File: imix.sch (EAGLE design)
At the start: 161 parts, among them Q1 AO3418, Q2 AO3415, Q3 AO3415, Q4 AO3415, Q5 AO3415, U1 BQ2423X, U10 ISL29035, U11 FX0S8700CQ, U12 296-12686-1-ND, U3 TLV3202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

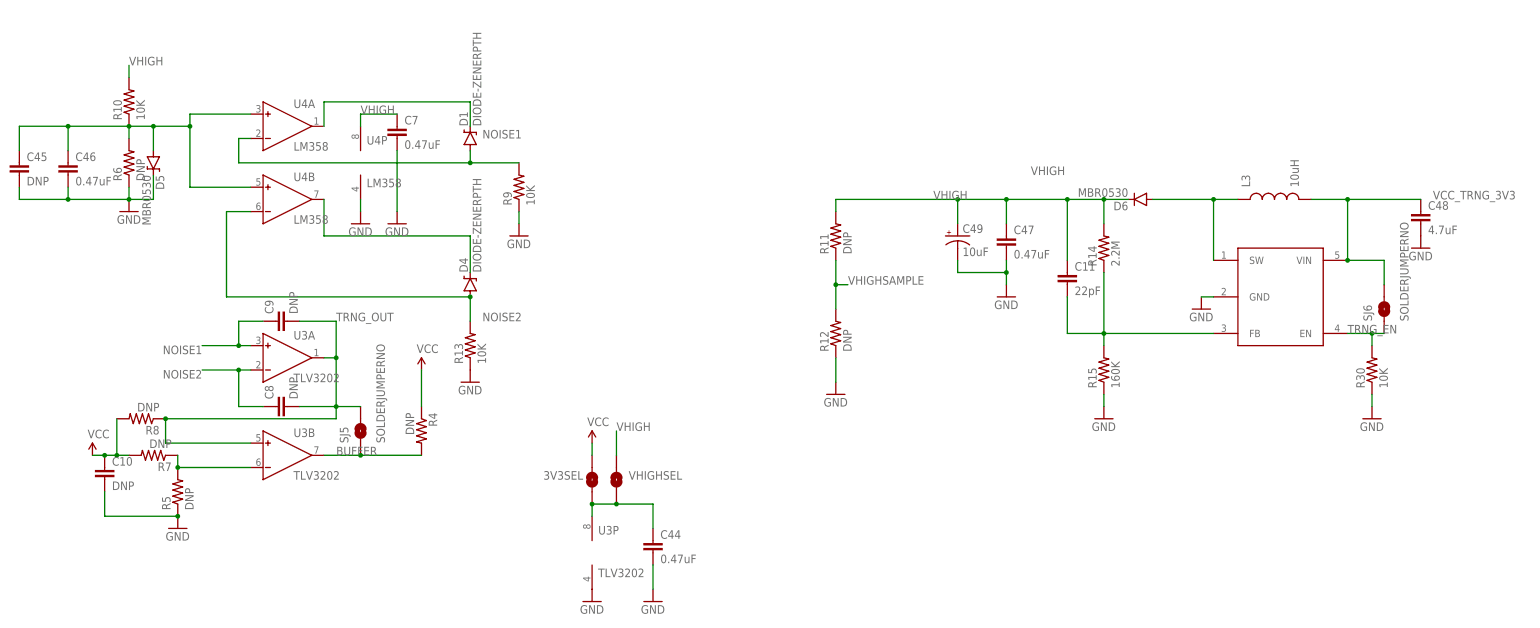
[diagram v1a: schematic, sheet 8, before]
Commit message: Refactor RNG
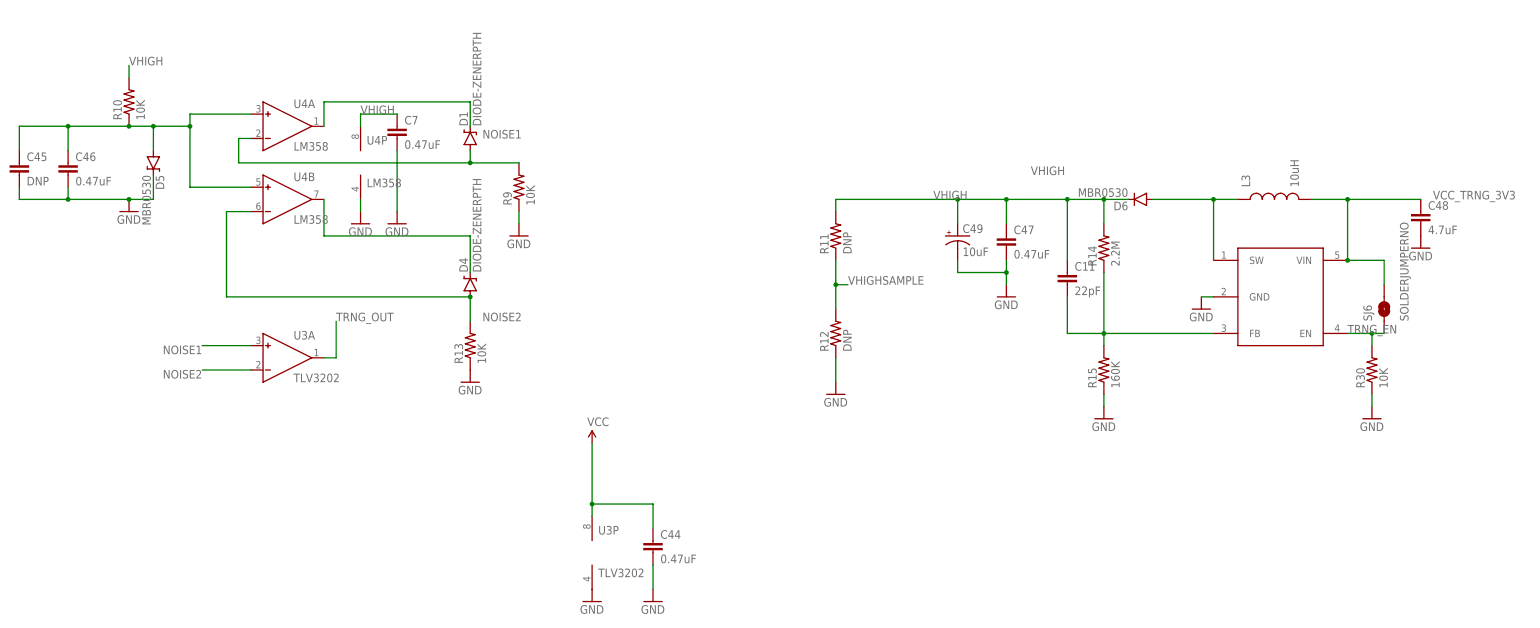
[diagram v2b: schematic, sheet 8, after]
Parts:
- removed 3V3SEL: SOLDERJUMPER-OLDTRACE, SparkFun-Retired:SOLDERJUMPER-OLDTRACE
- removed C10, C8, C9: DNP, SparkFun-Capacitors:CAP0603-CAP
- removed R4, R5, R7, R8: DNP, SparkFun-Passives:RESISTOR0603-RES
- removed R6: DNP, SparkFun-Resistors:RESISTOR0603
- removed SJ5: SOLDERJUMPERNO, SparkFun-Retired:SOLDERJUMPERNO
- removed VHIGHSEL: SOLDERJUMPER-OLDNO, SparkFun-Retired:SOLDERJUMPER-OLDNO
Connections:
- removed net BUFFER: R4.2, SJ5.1, U3B.OUT
- removed net N$67: R5.2, R7.1, U3B.IN-
- removed net N$68: 3V3SEL.1, C44.1, U3P.V+, VHIGHSEL.1
- net GND: no longer C10.2, R5.1, R6.1
- net N$66: no longer R6.2
- net NOISE1: no longer C9.1
- net NOISE2: no longer C8.1
- net TRNG_OUT: no longer C8.2, C9.2, R8.1, SJ5.2, U3B.IN+
- net VCC_TRNG_3V3: now also C44.1, U3P.V+; no longer 3V3SEL.2, C10.1, R4.1, R7.2, R8.2
- net VHIGH: no longer VHIGHSEL.2

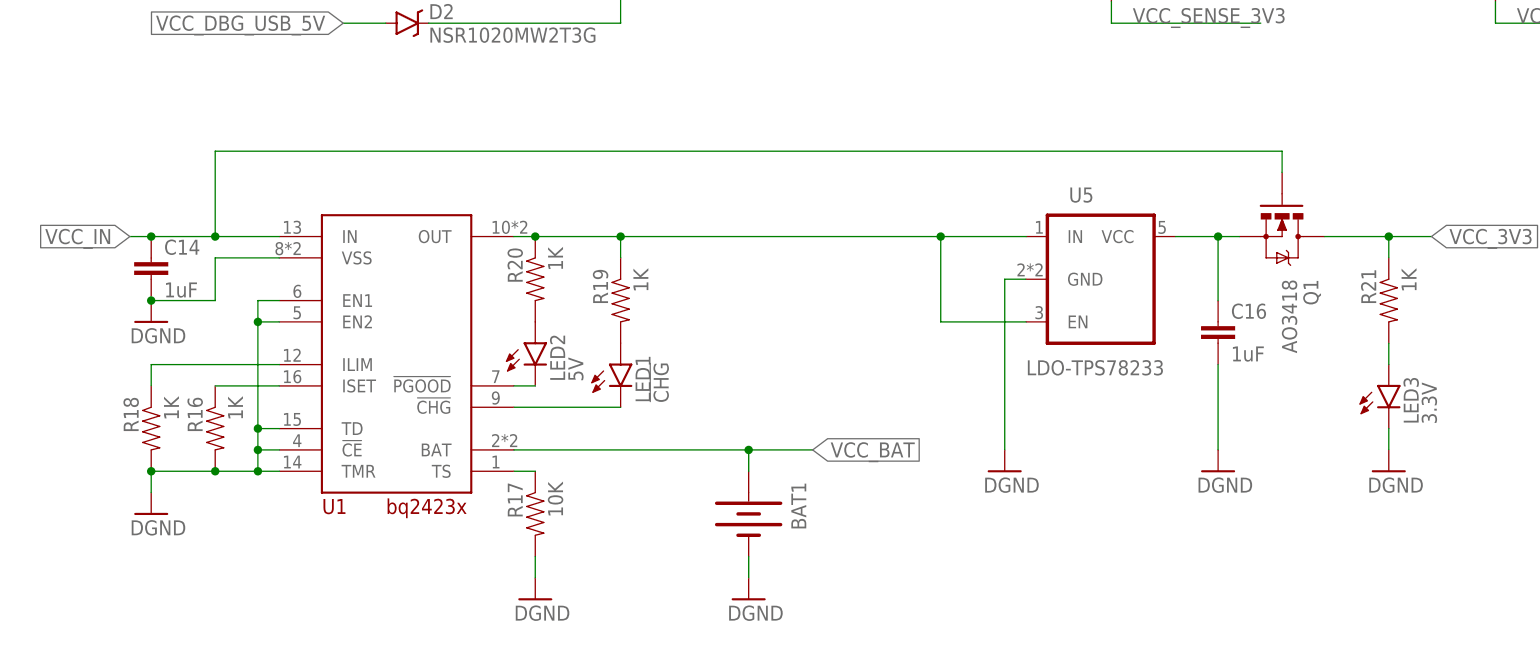
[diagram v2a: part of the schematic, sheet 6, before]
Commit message: Updated version incorporating several suggestions, still rerouting RNG
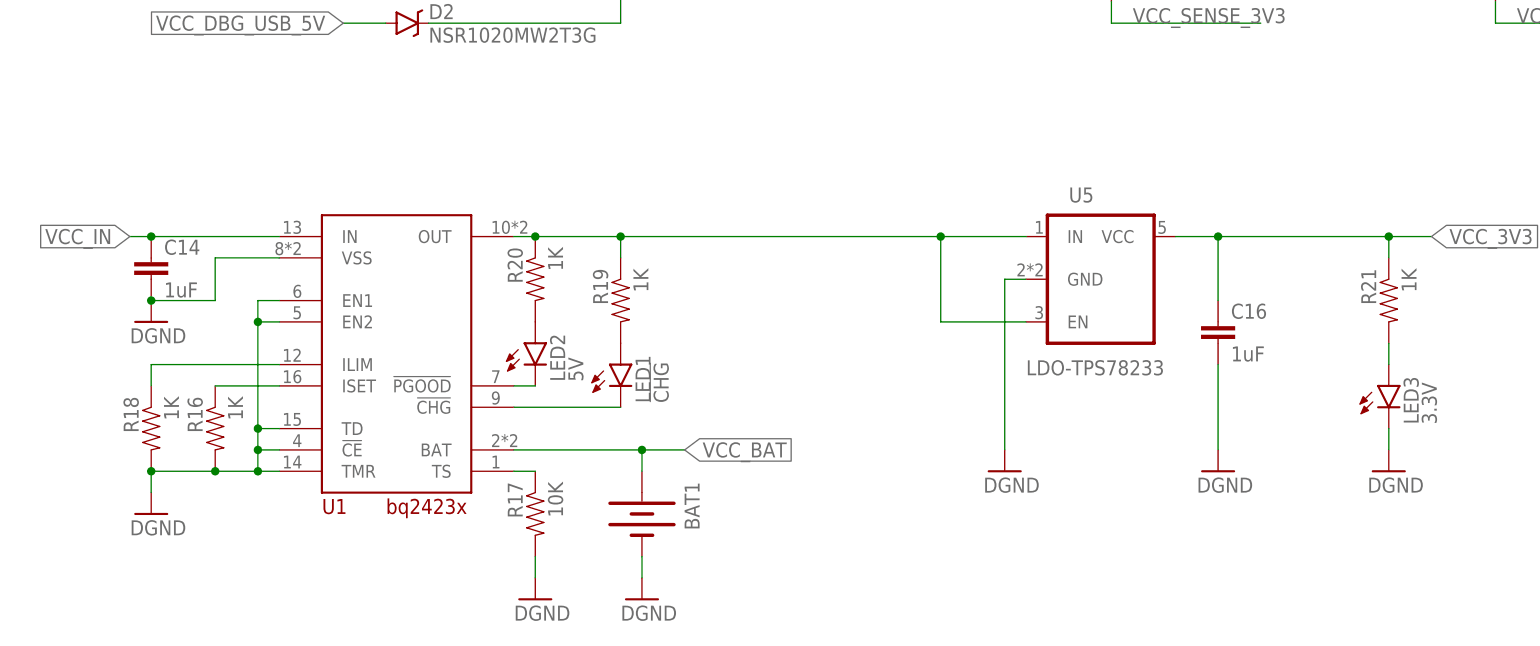
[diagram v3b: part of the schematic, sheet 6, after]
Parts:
- removed Q1: AO3418, SparkFun-DiscreteSemi:MOSFET-NCHANNELAO3404A
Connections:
- removed net VCC: C16.1, Q1.S, U5.VCC
- net VCC_3V3: now also C16.1, U5.VCC; no longer Q1.D
- net VCC_IN: no longer Q1.G
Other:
- moved on the sheet: BAT1
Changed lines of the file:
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@@
 <part name="U1" library="imix" deviceset="BQ2423X" device=""/>
 <part name="GND6" library="SparkFun-Aesthetics" deviceset="DGND" device=""/>
-<part name="Q1" library="SparkFun-DiscreteSemi" deviceset="MOSFET-NCHANNEL" device="AO3404A" value="AO3418"/>
 <part name="Q4" library="SparkFun-DiscreteSemi" deviceset="MOSFET-PCHANNEL" device="DMG2307L" value="AO3415"/>
 <part name="Q5" library="SparkFun-DiscreteSemi" deviceset="MOSFET-PCHANNEL" device="DMG2307L" value="AO3415"/>
@@
 <instance part="GND12" gate="G$1" x="81.28" y="5.08"/>
 <instance part="U1" gate="G$1" x="63.5" y="12.7"/>
-<instance part="GND6" gate="G$1" x="106.68" y="5.08"/>
-<instance part="Q1" gate="G$1" x="170.18" y="48.26" rot="R270"/>
+<instance part="GND6" gate="G$1" x="93.98" y="5.08"/>
 <instance part="Q4" gate="G$1" x="149.86" y="81.28" rot="MR180"/>
 <instance part="Q5" gate="G$1" x="195.58" y="81.28" rot="MR180"/>
@@
 <instance part="JP1" gate="G$1" x="274.32" y="91.44"/>
 <instance part="JP8" gate="G$1" x="231.14" y="66.04" rot="R270"/>
-<instance part="BAT1" gate="G$1" x="106.68" y="15.24" rot="R270"/>
+<instance part="BAT1" gate="G$1" x="93.98" y="15.24" rot="R270"/>
 </instances>
 <busses>
@@
 <pinref part="BAT1" gate="G$1" pin="-"/>
 <pinref part="GND6" gate="G$1" pin="GND"/>
-<wire x1="106.68" y1="10.16" x2="106.68" y2="7.62" width="0.1524" layer="91"/>
+<wire x1="93.98" y1="10.16" x2="93.98" y2="7.62" width="0.1524" layer="91"/>
 </segment>
 </net>
@@
 <segment>
 <pinref part="U1" gate="G$1" pin="BAT"/>
-<wire x1="78.74" y1="22.86" x2="106.68" y2="22.86" width="0.1524" layer="91"/>
-<label x="114.3" y="22.86" size="1.778" layer="95" xref="yes"/>
+<wire x1="78.74" y1="22.86" x2="93.98" y2="22.86" width="0.1524" layer="91"/>
+<label x="99.06" y="22.86" size="1.778" layer="95" xref="yes"/>
 <pinref part="BAT1" gate="G$1" pin="+"/>
-<wire x1="106.68" y1="22.86" x2="114.3" y2="22.86" width="0.1524" layer="91"/>
-<wire x1="106.68" y1="22.86" x2="106.68" y2="20.32" width="0.1524" layer="91"/>
-<junction x="106.68" y="22.86"/>
+<wire x1="93.98" y1="22.86" x2="99.06" y2="22.86" width="0.1524" layer="91"/>
+<wire x1="93.98" y1="22.86" x2="93.98" y2="20.32" width="0.1524" layer="91"/>
+<junction x="93.98" y="22.86"/>
 </segment>
 </net>
@@
 </net>
 <net name="VCC_3V3" class="1">
-<segment>
-<wire x1="182.88" y1="48.26" x2="187.96" y2="48.26" width="0.1524" layer="91"/>
-<pinref part="R21" gate="G$1" pin="1"/>
-<wire x1="182.88" y1="45.72" x2="182.88" y2="48.26" width="0.1524" layer="91"/>
-<label x="187.96" y="48.26" size="1.778" layer="95" xref="yes"/>
-<pinref part="Q1" gate="G$1" pin="D"/>
-<wire x1="175.26" y1="48.26" x2="182.88" y2="48.26" width="0.1524" layer="91"/>
-<junction x="182.88" y="48.26"/>
-</segment>
 <segment>
 <pinref part="SJ4" gate="G$1" pin="1"/>
@@
 <wire x1="281.94" y1="104.14" x2="241.3" y2="104.14" width="0.1524" layer="91"/>
 </segment>
+<segment>
+<pinref part="U5" gate="G$1" pin="VCC"/>
+<wire x1="157.48" y1="48.26" x2="162.56" y2="48.26" width="0.1524" layer="91"/>
+<pinref part="C16" gate="G$1" pin="1"/>
+<wire x1="162.56" y1="48.26" x2="162.56" y2="40.64" width="0.1524" layer="91"/>
+<junction x="162.56" y="48.26"/>
+<wire x1="182.88" y1="48.26" x2="187.96" y2="48.26" width="0.1524" layer="91"/>
+<pinref part="R21" gate="G$1" pin="1"/>
+<wire x1="182.88" y1="45.72" x2="182.88" y2="48.26" width="0.1524" layer="91"/>
+<label x="187.96" y="48.26" size="1.778" layer="95" xref="yes"/>
+<junction x="182.88" y="48.26"/>
+<wire x1="162.56" y1="48.26" x2="182.88" y2="48.26" width="0.1524" layer="91"/>
+</segment>
 </net>
 <net name="VCC_TARGET_USB_5V" class="1">
@@
 </segment>
 <segment>
-<wire x1="50.8" y1="48.26" x2="43.18" y2="48.26" width="0.1524" layer="91"/>
 <pinref part="C14" gate="G$1" pin="1"/>
-<wire x1="43.18" y1="48.26" x2="35.56" y2="48.26" width="0.1524" layer="91"/>
+<wire x1="50.8" y1="48.26" x2="35.56" y2="48.26" width="0.1524" layer="91"/>
 <wire x1="35.56" y1="48.26" x2="33.02" y2="48.26" width="0.1524" layer="91"/>
 <junction x="35.56" y="48.26"/>
 <label x="33.02" y="48.26" size="1.778" layer="95" rot="R180" xref="yes"/>
 <pinref part="U1" gate="G$1" pin="IN"/>
-<wire x1="43.18" y1="48.26" x2="43.18" y2="58.42" width="0.1524" layer="91"/>
-<junction x="43.18" y="48.26"/>
-<pinref part="Q1" gate="G$1" pin="G"/>
-<wire x1="43.18" y1="58.42" x2="170.18" y2="58.42" width="0.1524" layer="91"/>
-<wire x1="170.18" y1="58.42" x2="170.18" y2="55.88" width="0.1524" layer="91"/>
 </segment>
 </net>
@@
 </segment>
 </net>
-<net name="VCC" class="0">
-<segment>
-<pinref part="U5" gate="G$1" pin="VCC"/>
-<pinref part="Q1" gate="G$1" pin="S"/>
-<wire x1="157.48" y1="48.26" x2="162.56" y2="48.26" width="0.1524" layer="91"/>
-<pinref part="C16" gate="G$1" pin="1"/>
-<wire x1="162.56" y1="48.26" x2="165.1" y2="48.26" width="0.1524" layer="91"/>
-<wire x1="162.56" y1="48.26" x2="162.56" y2="40.64" width="0.1524" layer="91"/>
-<junction x="162.56" y="48.26"/>
-</segment>
-</net>

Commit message: DFM is almost passing
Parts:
- added F10, F7, F8, F9: FIDUCIAL, GeekAmmo:FIDUCIAL
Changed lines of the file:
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@@
 <part name="R30" library="SparkFun-Resistors" deviceset="RESISTOR" device="0603" value="10K"/>
 <part name="GND56" library="SparkFun-Aesthetics" deviceset="GND" device=""/>
+<part name="F7" library="GeekAmmo" deviceset="FIDUCIAL" device=""/>
+<part name="F8" library="GeekAmmo" deviceset="FIDUCIAL" device=""/>
+<part name="F9" library="GeekAmmo" deviceset="FIDUCIAL" device=""/>
+<part name="F10" library="GeekAmmo" deviceset="FIDUCIAL" device=""/>
 </parts>
 <sheets>
@@
 <instance part="F5" gate="G$1" x="88.9" y="58.42"/>
 <instance part="F6" gate="G$1" x="99.06" y="60.96"/>
+<instance part="F7" gate="G$1" x="96.52" y="45.72"/>
+<instance part="F8" gate="G$1" x="86.36" y="40.64"/>
+<instance part="F9" gate="G$1" x="96.52" y="33.02"/>
+<instance part="F10" gate="G$1" x="86.36" y="30.48"/>
 </instances>
 <busses>
